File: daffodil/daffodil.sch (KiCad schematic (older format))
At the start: 9 parts, among them J1 NEIGHBOR1, J2 NEIGHBOR2, J3 BREADBOARD, J7 BONUS_ROW, P1 GREATFET-PROTO-AREA

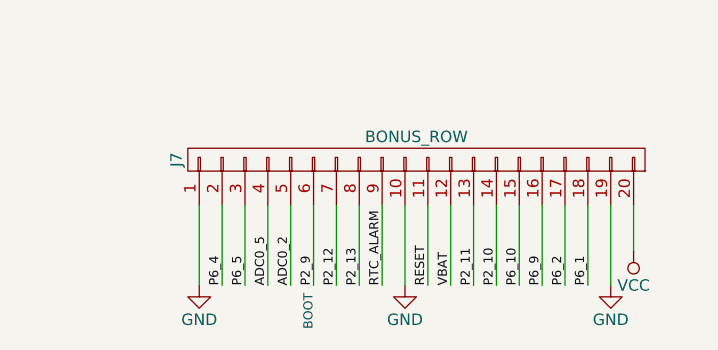
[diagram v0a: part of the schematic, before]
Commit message: Daffodil: removed GND from J7 pin 10, updated silkscreen
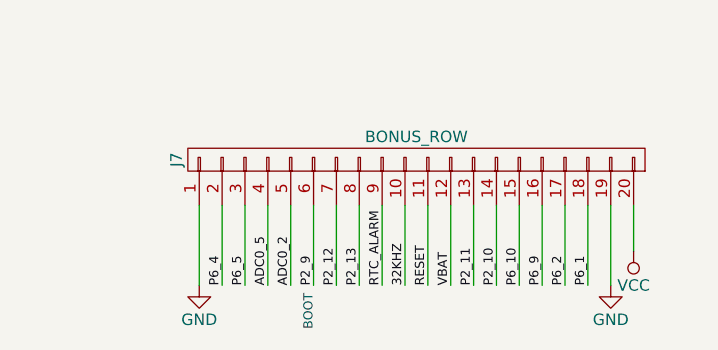
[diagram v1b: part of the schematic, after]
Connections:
- net GND: no longer J7.10 (P10)
- new net 32KHZ: J7.10 (P10)
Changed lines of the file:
@@
-$EndComp
-$Comp
-L GND #PWR011
-U 1 1 56036BE7
-P 15150 7550
-F 0 "#PWR011" H 15150 7300 50  0001 C CNN
-F 1 "GND" H 15150 7400 50  0000 C CNN
-F 2 "" H 15150 7550 60  0000 C CNN
-F 3 "" H 15150 7550 60  0000 C CNN
-	1    15150 7550
-	1    0    0    -1
 $EndComp
 $Comp
@@
 	1    0    0    -1
 $EndComp
+Text Label 15150 7550 1    40   ~ 0
+32KHZ
 $EndSCHEMATC

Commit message: Updated Daffodil silkscreen, porto area, and breadboard.
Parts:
- J1, J2: symbol CONN_02X20 -> daffodil-rescue:CONN_02X20
- J3: symbol HEATSINK -> daffodil-rescue:HEATSINK; Manufacturer Parallax -> SparkFun Electronics; Part Number 700-00012 -> PRT-12047
- J7: symbol CONN_01X20 -> daffodil-rescue:CONN_01X20
- MH1, MH2, MH3, MH4: symbol CONN_01X01 -> daffodil-rescue:CONN_01X01
- P1: symbol GREATFET-PROTO-AREA -> gsg-symbols:GREATFET-PROTO-AREA
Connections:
- net GND: no longer P1.14, P1.15
- net VBUS: now also P1.14, P1.15; no longer P1.19, P1.20, P1.21, P1.22
- net VCC: now also P1.19, P1.20, P1.21, P1.22; no longer P1.25, P1.26, P1.27, P1.28, P1.29, P1.30
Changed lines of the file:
@@
-EESchema Schematic File Version 2
-LIBS:power
-LIBS:device
-LIBS:transistors
-LIBS:conn
-LIBS:linear
-LIBS:regul
-LIBS:74xx
-LIBS:cmos4000
-LIBS:adc-dac
-LIBS:memory
-LIBS:xilinx
-LIBS:microcontrollers
-LIBS:dsp
-LIBS:microchip
-LIBS:analog_switches
-LIBS:motorola
-LIBS:texas
-LIBS:intel
-LIBS:audio
-LIBS:interface
-LIBS:digital-audio
-LIBS:philips
-LIBS:display
-LIBS:cypress
-LIBS:siliconi
-LIBS:opto
-LIBS:atmel
-LIBS:contrib
-LIBS:valves
-LIBS:gsg-symbols
+EESchema Schematic File Version 4
 LIBS:daffodil-cache
-EELAYER 25 0
+EELAYER 26 0
 EELAYER END
 $Descr USLedger 17000 11000
@@
 P2_8
 $Comp
-L CONN_02X20 J2
+L daffodil-rescue:CONN_02X20 J2
 U 1 1 55EAB4B7
 P 15750 2650
@@
 $EndComp
 $Comp
-L GND #PWR01
+L power:GND #PWR01
 U 1 1 55EACE84
 P 15300 1700
@@
 $EndComp
 $Comp
-L GND #PWR02
+L power:GND #PWR02
 U 1 1 55EAECD0
 P 15300 4300
@@
 $EndComp
 $Comp
-L VCC #PWR03
+L power:VCC #PWR03
 U 1 1 55EAF03E
 P 16200 4300
@@
 VBUS
 $Comp
-L CONN_02X20 J1
+L daffodil-rescue:CONN_02X20 J1
 U 1 1 55FB1D52
 P 15750 5250
@@
 P2_13
 $Comp
-L GND #PWR04
+L power:GND #PWR04
 U 1 1 560E00A9
 P 14250 7550
@@
 $EndComp
 $Comp
-L VCC #PWR05
+L power:VCC #PWR05
 U 1 1 560E046D
 P 16150 7400
@@
 BOOT
 $Comp
-L CONN_01X20 J7
+L daffodil-rescue:CONN_01X20 J7
 U 1 1 560E713A
 P 15200 7000
@@
 ADC0_5
 $Comp
-L CONN_01X01 MH3
+L daffodil-rescue:CONN_01X01 MH3
 U 1 1 5600EED5
 P 13650 850
@@
 $EndComp
 $Comp
-L GND #PWR06
+L power:GND #PWR06
 U 1 1 5600F9D3
 P 13650 1150
@@
 $EndComp
 $Comp
-L CONN_01X01 MH4
+L daffodil-rescue:CONN_01X01 MH4
 U 1 1 560100F3
 P 14150 1000
@@
 $EndComp
 $Comp
-L GND #PWR07
+L power:GND #PWR07
 U 1 1 560100F9
 P 14150 1300
@@
 $EndComp
 $Comp
-L CONN_01X01 MH1
+L daffodil-rescue:CONN_01X01 MH1
 U 1 1 56010ADB
 P 12650 850
@@
 $EndComp
 $Comp
-L GND #PWR08
+L power:GND #PWR08
 U 1 1 56010AE1
 P 12650 1150
@@
 $EndComp
 $Comp
-L CONN_01X01 MH2
+L daffodil-rescue:CONN_01X01 MH2
 U 1 1 56010AE9
 P 13150 1000
@@
 $EndComp
 $Comp
-L GND #PWR09
+L power:GND #PWR09
 U 1 1 56010AEF
 P 13150 1300
@@
 RTC_ALARM
 $Comp
-L GND #PWR010
+L power:GND #PWR010
 U 1 1 56035FE9
 P 16050 7550
@@
 $EndComp
 $Comp
-L GND #PWR012
+L power:GND #PWR012
 U 1 1 560892BC
 P 8450 5500
@@
 $EndComp
 $Comp
-L VCC #PWR013
+L power:VCC #PWR013
 U 1 1 56089F65
 P 8250 5500
@@
 	8350 4000 8450 4000
 Wire Wire Line
-	8450 4000 8450 5500
+	8450 4000 8450 4100
 Wire Wire Line
 	8350 4100 8450 4100
@@
 Connection ~ 8450 4500
 Wire Wire Line
-	8350 4600 8450 4600
-Connection ~ 8450 4600
-Wire Wire Line
-	8450 4700 8350 4700
-Connection ~ 8450 4700
-Wire Wire Line
 	8350 4800 8450 4800
 Connection ~ 8450 4800
@@
 Connection ~ 8450 5400
 Wire Wire Line
-	8250 5500 8250 4700
-Wire Wire Line
-	8250 4700 8150 4700
-Wire Wire Line
-	8250 3750 8250 4600
-Wire Wire Line
-	8250 4600 8150 4600
-Wire Wire Line
-	8150 4500 8250 4500
-Connection ~ 8250 4500
+	8250 5500 8250 5400
+Wire Wire Line
+	8250 3750 8250 4000
 Wire Wire Line
 	8250 4400 8150 4400
-Connection ~ 8250 4400
 Wire Wire Line
 	8150 4300 8250 4300
@@
 Connection ~ 8250 4000
 Wire Wire Line
-	8150 4800 8250 4800
-Connection ~ 8250 4800
-Wire Wire Line
 	8250 4900 8150 4900
-Connection ~ 8250 4900
 Wire Wire Line
 	8150 5000 8250 5000
@@
 Connection ~ 8250 5400
 $Comp
-L GREATFET-PROTO-AREA P1
+L daffodil-rescue:HEATSINK J3
+U 1 1 569FDCB2
+P 7900 7500
+F 0 "J3" H 7900 7700 50  0000 C CNN
+F 1 "BREADBOARD" H 7900 7450 50  0000 C CNN
+F 2 "" H 7900 7500 60  0000 C CNN
+F 3 "" H 7900 7500 60  0000 C CNN
+F 4 "SparkFun Electronics" H 7900 7500 60  0001 C CNN "Manufacturer"
+F 5 "PRT-12047" H 7900 7500 60  0001 C CNN "Part Number"
+F 6 "BREADBOARD SOLDERLESS" H 7900 7500 60  0001 C CNN "Description"
+	1    7900 7500
+	1    0    0    -1
+$EndComp
+Text Label 15150 7550 1    40   ~ 0
+32KHZ
+Wire Wire Line
+	8450 4100 8450 4200
+Wire Wire Line
+	8450 4200 8450 4300
+Wire Wire Line
+	8450 4300 8450 4400
+Wire Wire Line
+	8450 4400 8450 4500
+Wire Wire Line
+	8450 4800 8450 4900
+Wire Wire Line
+	8450 4900 8450 5000
+Wire Wire Line
+	8450 5000 8450 5100
+Wire Wire Line
+	8450 5100 8450 5200
+Wire Wire Line
+	8450 5200 8450 5300
+Wire Wire Line
+	8450 5300 8450 5400
+Wire Wire Line
+	8450 5400 8450 5500
+Wire Wire Line
+	8250 4300 8250 4400
+Wire Wire Line
+	8250 4200 8250 4300
+Wire Wire Line
+	8250 4100 8250 4200
+Wire Wire Line
+	8250 4000 8250 4100
+Wire Wire Line
+	8250 5000 8250 4900
+Wire Wire Line
+	8250 5100 8250 5000
+Wire Wire Line
+	8250 5200 8250 5100
+Wire Wire Line
+	8250 5300 8250 5200
+Wire Wire Line
+	8250 5400 8250 5300
+Wire Wire Line
+	8450 4500 8450 4800
+$Comp
+L gsg-symbols:GREATFET-PROTO-AREA P1
 U 1 1 56085DCC
 P 8350 4700
@@
 	1    0    0    -1
 $EndComp
-$Comp
-L HEATSINK J3
-U 1 1 569FDCB2
-P 7900 7500
-F 0 "J3" H 7900 7700 50  0000 C CNN
-F 1 "BREADBOARD" H 7900 7450 50  0000 C CNN
-F 2 "" H 7900 7500 60  0000 C CNN
-F 3 "" H 7900 7500 60  0000 C CNN
-F 4 "Parallax" H 7900 7500 60  0001 C CNN "Manufacturer"
-F 5 "700-00012" H 7900 7500 60  0001 C CNN "Part Number"
-F 6 "BREADBOARD SOLDERLESS" H 7900 7500 60  0001 C CNN "Description"
-	1    7900 7500
-	1    0    0    -1
-$EndComp
-Text Label 15150 7550 1    40   ~ 0
-32KHZ
 $EndSCHEMATC
